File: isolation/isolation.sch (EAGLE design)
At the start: 29 parts, among them IC1 XTLV61048DBVR, IC2 SN74HC14DRG3, J1 S4B-XH-A_LF__SN_, J2 S4B-XH-A_LF__SN_

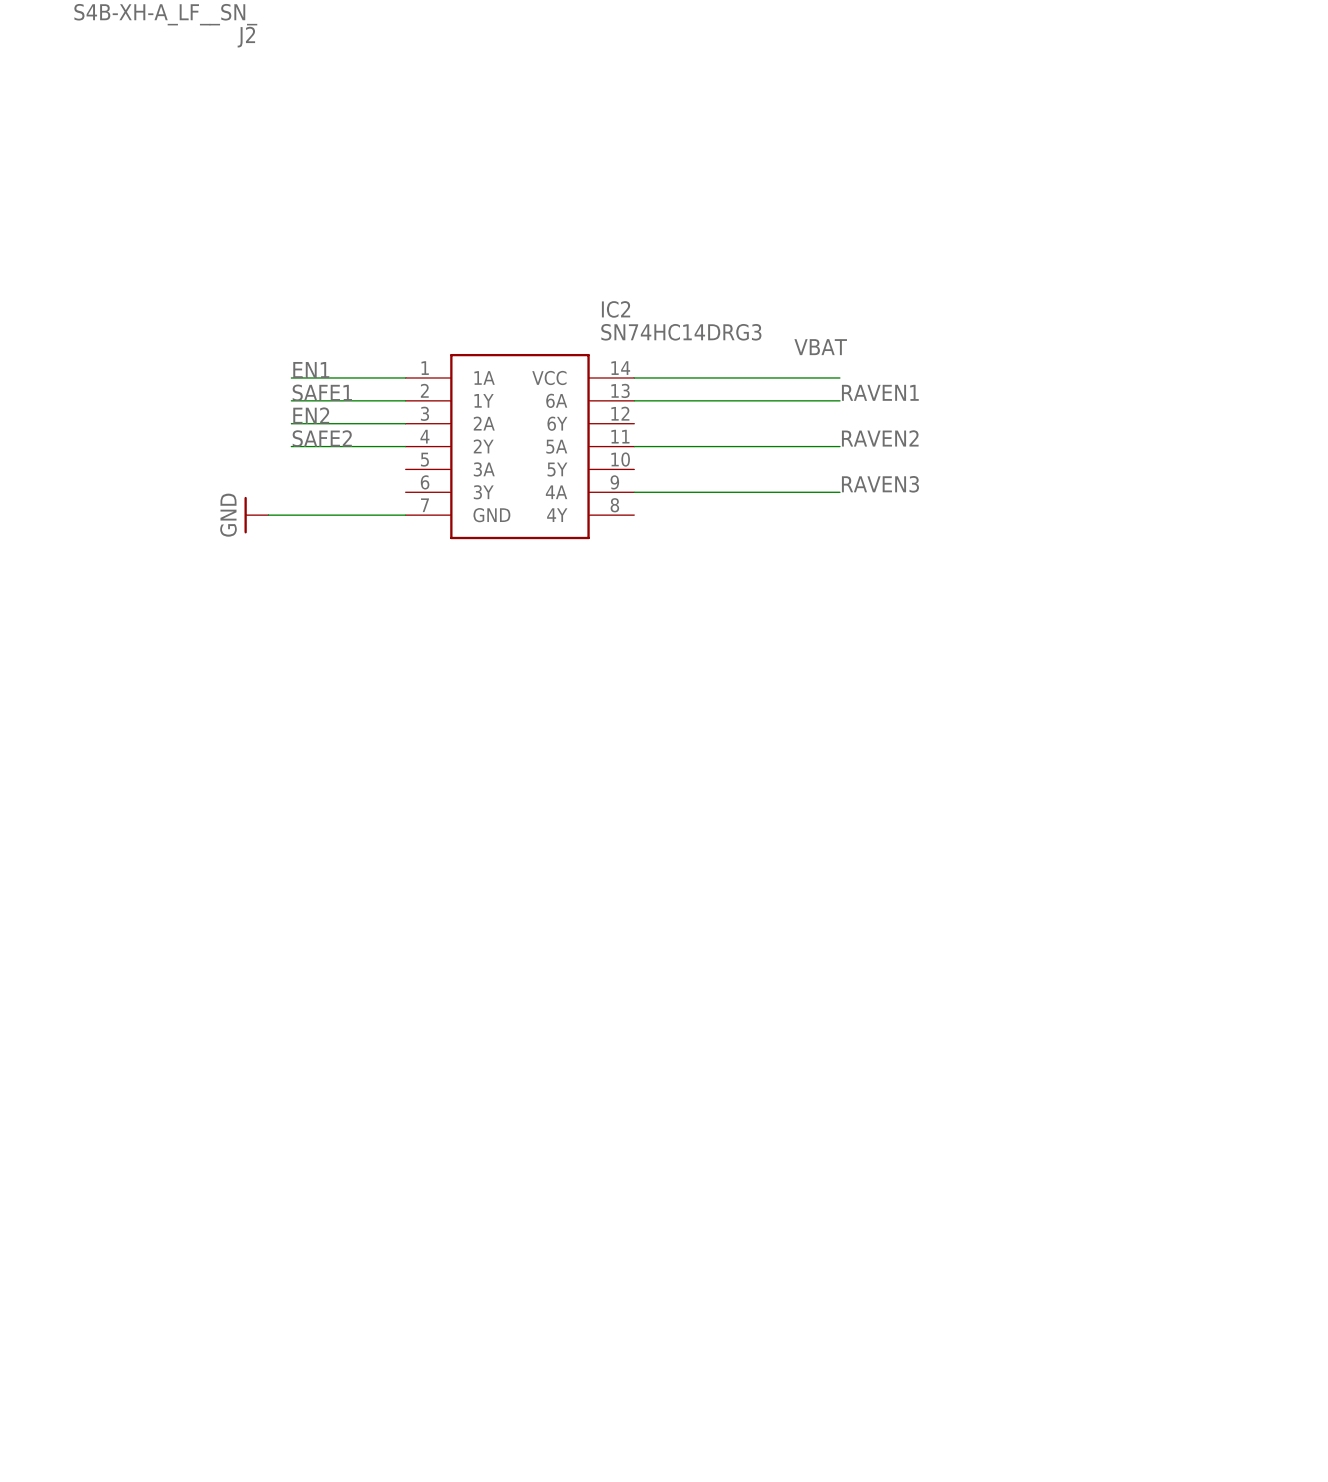
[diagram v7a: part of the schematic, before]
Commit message: complete firing logic
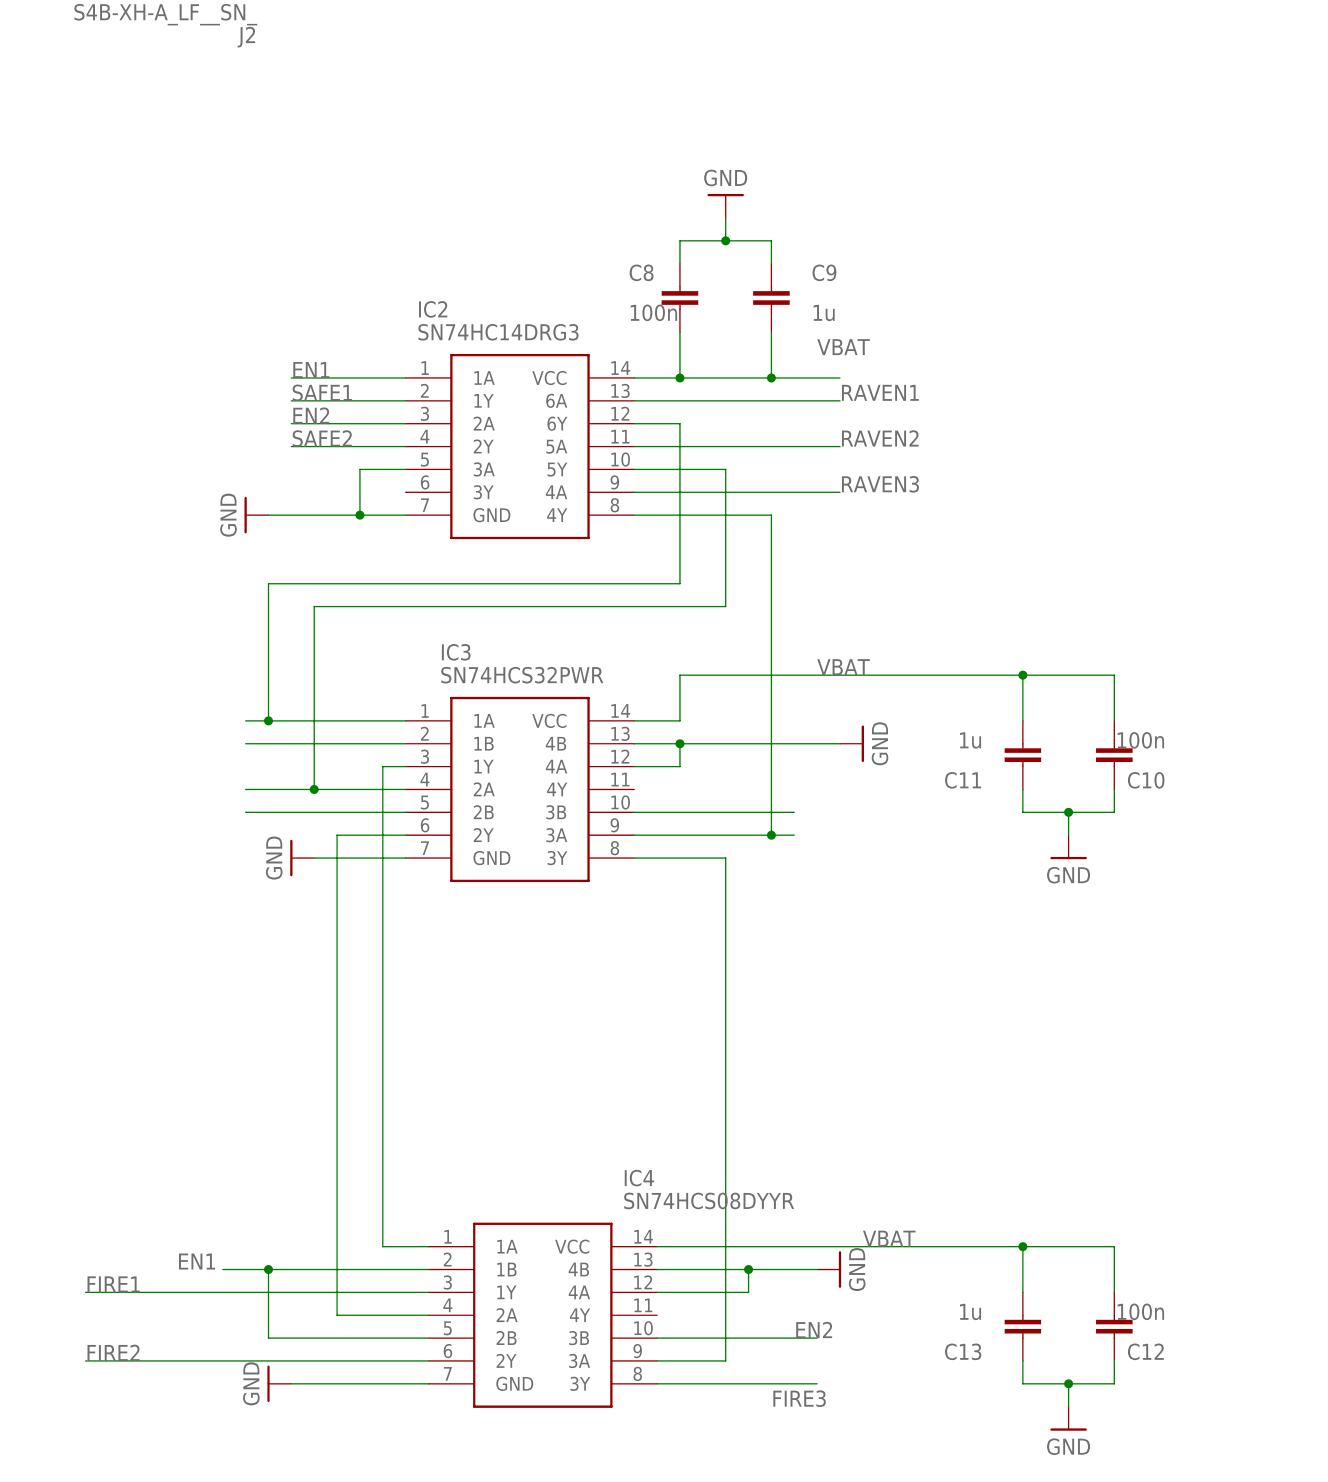
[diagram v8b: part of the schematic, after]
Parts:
- added C10, C12, C8: 100n, Capacitor:C_CHIP-0603(1608-METRIC)
- added C11, C13, C9: 1u, Capacitor:C_CHIP-0603(1608-METRIC)
- added IC3: SN74HCS32PWR, SamacSys_Parts:SN74HCS32PWR
- added IC4: SN74HCS08DYYR, SamacSys_Parts:SN74HCS08DYYR
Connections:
- new net FIRE1: IC4.1Y
- new net FIRE2: IC4.2Y
- new net FIRE3: IC4.3Y
- new net N$10: IC2.5Y, IC3.2A
- new net N$11: IC3.2B
- new net N$12: IC3.3B
- new net N$13: IC2.4Y, IC3.3A
- new net N$14: IC3.3Y, IC4.3A
- new net N$15: IC3.1Y, IC4.1A
- new net N$16: IC3.2Y, IC4.2A
- new net N$8: IC2.6Y, IC3.1A
- new net N$9: IC3.1B
- net EN1: now also IC4.1B, IC4.2B
- net EN2: now also IC4.3B
- net GND: now also C10.1, C11.1, C12.1, C13.1, C8.1, C9.1, IC2.3A, IC3.4A, IC3.4B, IC3.GND, IC4.4A, IC4.4B, IC4.GND
- net VBAT: now also C10.2, C11.2, C12.2, C13.2, C8.2, C9.2, IC3.VCC, IC4.VCC
